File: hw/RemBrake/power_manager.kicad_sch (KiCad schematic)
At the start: 22 parts, among them IC1 LTC2943IDD#TRPBF, Q10 BC337, Q11 BC847, U7 MAX40200AUK, U8 MAX40200AUK

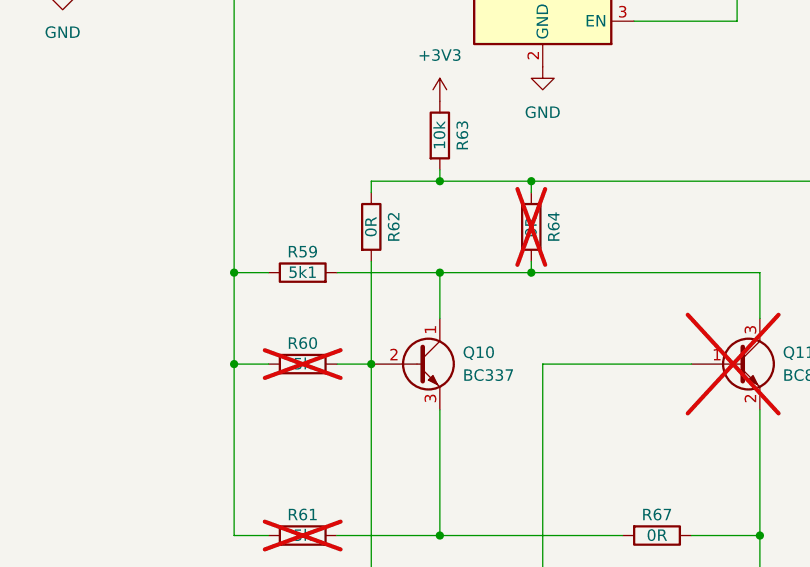
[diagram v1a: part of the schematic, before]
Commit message: adjusted connections to be able to use bc337
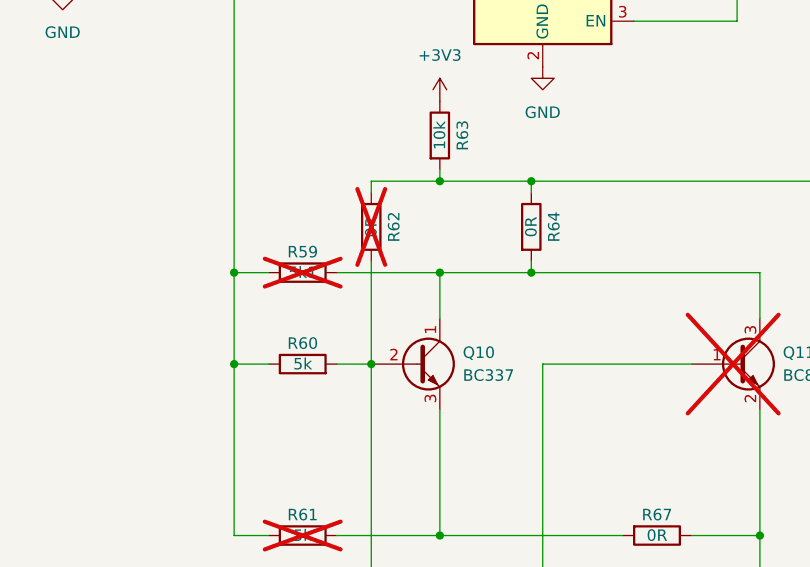
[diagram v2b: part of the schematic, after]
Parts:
- R59, R62: now not fitted; now left out of the parts list
- R60, R64: now fitted; now in the parts list
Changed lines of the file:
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@@
 (kicad_sch
-	(version 20250318)
+	(version 20250513)
 	(generator "eeschema")
 	(generator_version "9.99")
@@
 		(unit 1)
 		(exclude_from_sim no)
-		(in_bom yes)
+		(in_bom no)
 		(on_board yes)
-		(dnp no)
+		(dnp yes)
 		(property "Reference" "R62"
 			(at 195.58 97.79 90)
@@
 		(unit 1)
 		(exclude_from_sim no)
-		(in_bom yes)
+		(in_bom no)
 		(on_board yes)
-		(dnp no)
+		(dnp yes)
 		(property "Reference" "R59"
 			(at 185.42 100.584 90)
@@
 		(unit 1)
 		(exclude_from_sim no)
-		(in_bom no)
+		(in_bom yes)
 		(on_board yes)
-		(dnp yes)
+		(dnp no)
 		(property "Reference" "R60"
 			(at 185.42 110.744 90)
@@
 		(dnp no)
 		(fields_autoplaced yes)
-		(property "Height" "0.8"
-			(at 52.07 -337.77 0)
-			(hide yes)
+		(property "Reference" "IC1"
+			(at 83.82 68.58 0)
 			(effects
 				(font
 					(size 1.27 1.27)
 				)
-				(justify left top)
 			)
 		)
-		(property "Mouser Part Number" "584-LTC2943IDD#TRPBF"
-			(at 52.07 -437.77 0)
-			(hide yes)
+		(property "Value" "LTC2943IDD#TRPBF"
+			(at 83.82 71.12 0)
 			(effects
 				(font
 					(size 1.27 1.27)
 				)
-				(justify left top)
 			)
 		)
-		(property "Mouser Price/Stock" "https://www.mouser.co.uk/ProductDetail/Analog-Devices/LTC2943IDDTRPBF?qs=hVkxg5c3xu8j%252BJ6DK3jV8w%3D%3D"
-			(at 52.07 -537.77 0)
+		(property "Footprint" "Package_DFN_QFN:DFN-8-1EP_3x3mm_P0.5mm_EP1.66x2.38mm"
+			(at 52.07 -37.77 0)
 			(hide yes)
 			(effects
@@
 			)
 		)
-		(property "Manufacturer_Name" "Analog Devices"
-			(at 52.07 -637.77 0)
+		(property "Datasheet" "https://www.mouser.in/datasheet/2/609/2943fa-1271567.pdf"
+			(at 52.07 -137.77 0)
 			(hide yes)
 			(effects
@@
 			)
 		)
-		(property "Manufacturer_Part_Number" "LTC2943IDD#TRPBF"
-			(at 52.07 -737.77 0)
+		(property "Description" "Battery Management 20V Battery Gas Gauge with Voltage, Current & Temperature Measurement"
+			(at 83.82 57.15 0)
 			(hide yes)
 			(effects
@@
 					(size 1.27 1.27)
 				)
-				(justify left top)
 			)
 		)
-		(property "Reference" "IC1"
-			(at 83.82 68.58 0)
+		(property "Height" "0.8"
+			(at 52.07 -337.77 0)
+			(hide yes)
 			(effects
 				(font
 					(size 1.27 1.27)
 				)
+				(justify left top)
 			)
 		)
-		(property "Value" "LTC2943IDD#TRPBF"
-			(at 83.82 71.12 0)
+		(property "Mouser Part Number" "584-LTC2943IDD#TRPBF"
+			(at 52.07 -437.77 0)
+			(hide yes)
 			(effects
 				(font
 					(size 1.27 1.27)
 				)
+				(justify left top)
 			)
 		)
-		(property "Footprint" "Package_DFN_QFN:DFN-8-1EP_3x3mm_P0.5mm_EP1.66x2.38mm"
-			(at 52.07 -37.77 0)
+		(property "Mouser Price/Stock" "https://www.mouser.co.uk/ProductDetail/Analog-Devices/LTC2943IDDTRPBF?qs=hVkxg5c3xu8j%252BJ6DK3jV8w%3D%3D"
+			(at 52.07 -537.77 0)
 			(hide yes)
 			(effects
@@
 			)
 		)
-		(property "Datasheet" "https://www.mouser.in/datasheet/2/609/2943fa-1271567.pdf"
-			(at 52.07 -137.77 0)
+		(property "Manufacturer_Name" "Analog Devices"
+			(at 52.07 -637.77 0)
 			(hide yes)
 			(effects
@@
 			)
 		)
-		(property "Description" "Battery Management 20V Battery Gas Gauge with Voltage, Current & Temperature Measurement"
-			(at 83.82 57.15 0)
+		(property "Manufacturer_Part_Number" "LTC2943IDD#TRPBF"
+			(at 52.07 -737.77 0)
 			(hide yes)
 			(effects
@@
 					(size 1.27 1.27)
 				)
+				(justify left top)
 			)
 		)
@@
 		(unit 1)
 		(exclude_from_sim no)
-		(in_bom no)
+		(in_bom yes)
 		(on_board yes)
-		(dnp yes)
+		(dnp no)
 		(property "Reference" "R64"
 			(at 213.36 97.79 90)

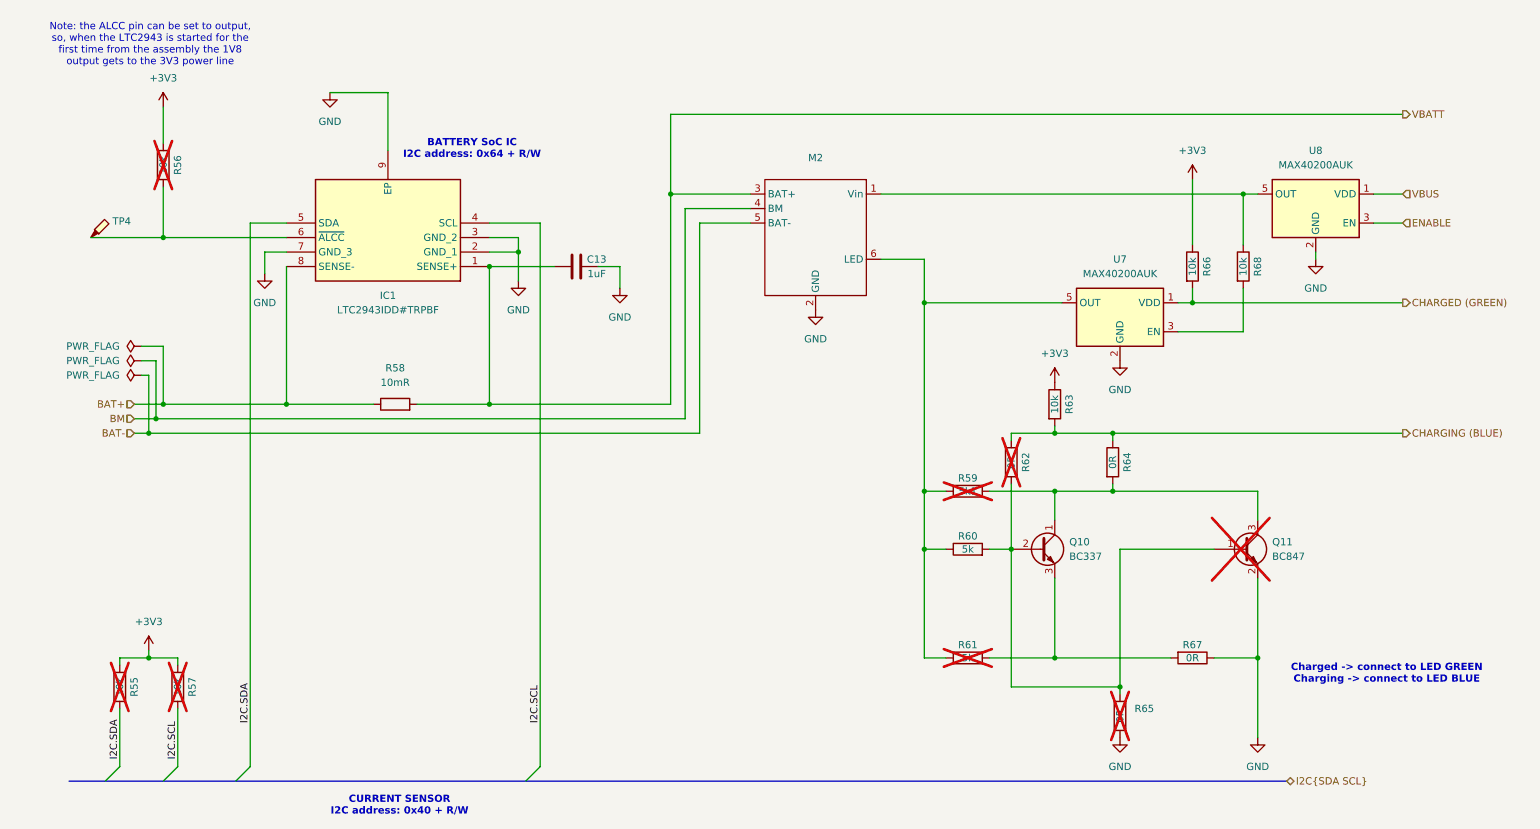
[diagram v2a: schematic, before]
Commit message: finished todos - prepared for routing
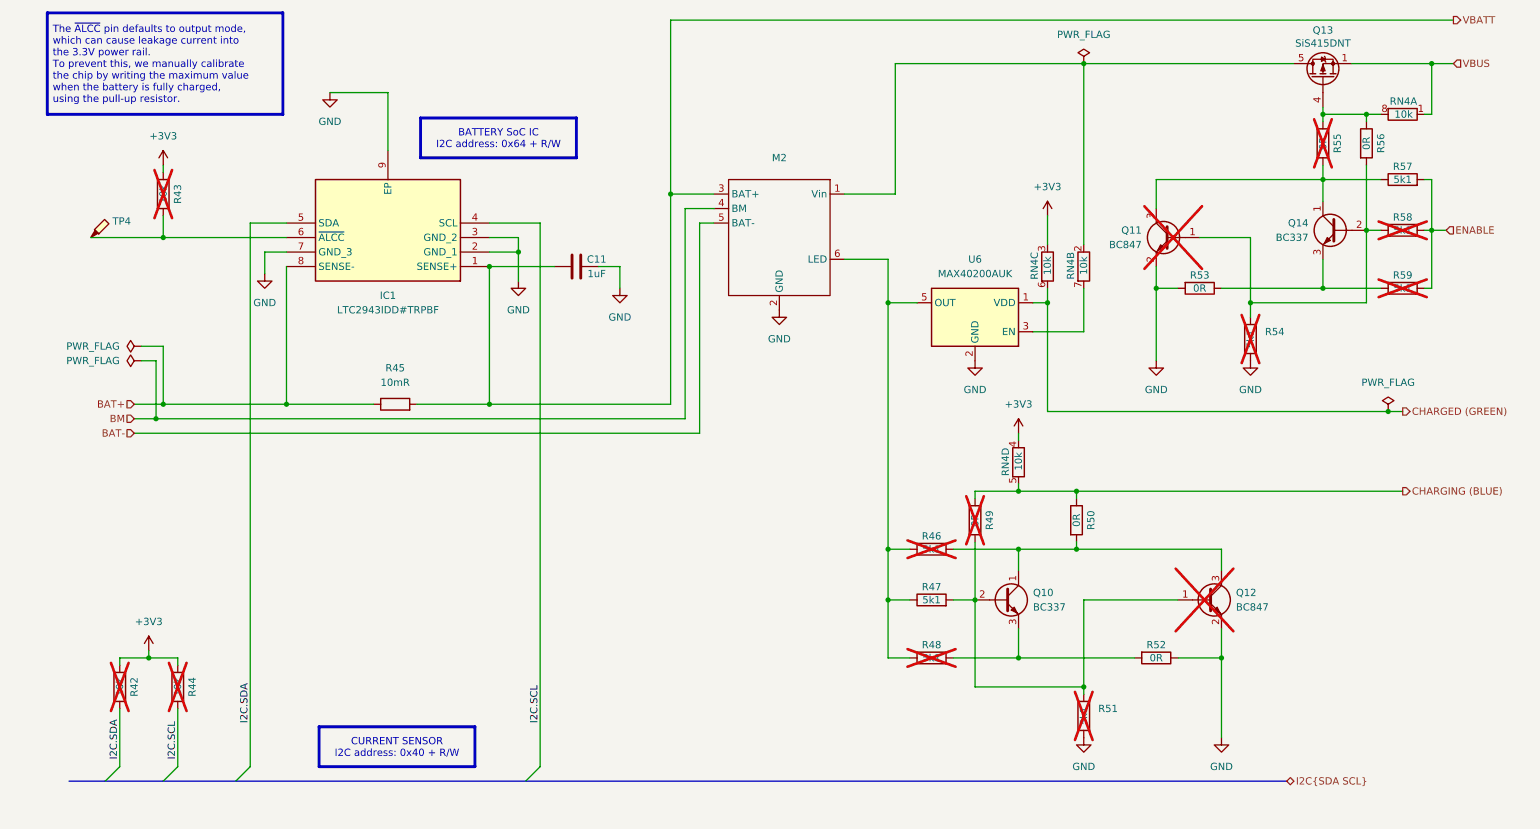
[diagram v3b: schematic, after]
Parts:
- removed R63, R66, R68: 10k, Resistor_SMD:R_0805_2012Metric_Pad1.20x1.40mm_HandSolder, symbol Device:R
- removed U8: MAX40200AUK, Package_TO_SOT_SMD:SOT-23-5, symbol Analog_Switch:MAX40200AUK
- added Q11: BC847, Package_TO_SOT_SMD:SOT-23, symbol Transistor_BJT:BC847
- added Q13: SiS415DNT, Package_SO:Vishay_PowerPAK_1212-8_Single, symbol Transistor_FET:SiS415DNT
- added Q14: BC337, Package_TO_SOT_THT:TO-92_Inline, symbol Transistor_BJT:BC337
- added R53, R55, R56: 0R, Resistor_SMD:R_0805_2012Metric_Pad1.20x1.40mm_HandSolder, symbol Device:R
- added R54, R57, R58, R59: 5k1, Resistor_SMD:R_0805_2012Metric_Pad1.20x1.40mm_HandSolder, symbol Device:R
- added RN4: 10k, Resistor_SMD:R_Array_Convex_4x0603, symbol Device:R_Pack04_Split
- R47: renamed from R60; value 5k -> 5k1
- R48: renamed from R61; value 5k -> 5k1
- R51: renamed from R65; value 0R -> 5k1
- renumbered C13 to C11, Q11 to Q12, R55 to R42, R56 to R43, R57 to R44, R58 to R45, R59 to R46, R62 to R49, R64 to R50, R67 to R52, U7 to U6
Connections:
- net +3V3: now also RN4.3 (R3.1), RN4.4 (R4.1)
- net CHARGED (GREEN): now also RN4.6 (R3.2)
- net CHARGING (BLUE): now also RN4.5 (R4.2)
- net ENABLE: now also R57.2, R58.2, R59.2
- net GND: now also Q11.2 (E), R53.2, R54.1
- net VBUS: now also Q13.1 (S), Q13.2 (S), Q13.3 (S), RN4.1 (R1.1)
- net at M2.1 (Vin): now also Q13.5 (D), RN4.2 (R2.1)
- net at U6.3 (EN): now also RN4.7 (R2.2)
- new net: Q13.4 (G), R55.1, R56.1, RN4.8 (R1.2)
- new net: Q11.3 (C), Q14.1 (C), R55.2, R57.1
- new net: Q14.3 (E), R53.1, R59.1
- new net: Q11.1 (B), Q14.2 (B), R54.2, R56.2, R58.1
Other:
- note removed: "BATTERY SoC IC I2C address: 0x64 + R/W"
- note removed: "CURRENT SENSOR I2C address: 0x40 + R/W"
- note removed: "Charged -> connect to LED GREEN Charging -> connect to LED BLUE"
- note removed: "Note: the ALCC pin can be set to output, so, when the LTC2943 is started for the first time from the assembly the 1V8 output gets to the 3V3 power line"
- moved on the sheet: M2, Q10, R43, R46, R47, R48, R49, R50, R51, R52, U6

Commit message: new routing version 3.0 with power mosfet swich for the charger and fixed problems with LED and buzzer reset delayed circuit
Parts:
- renumbered C11 to C13, R42 to R48, R43 to R49, R44 to R50, R45 to R51, R46 to R52, R47 to R53, R48 to R54, R49 to R55, R50 to R56, R51 to R57, R52 to R58, R53 to R59, R54 to R60, R55 to R61, R56 to R62, R57 to R63, R58 to R64, R59 to R65, U6 to U7
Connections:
- net +3V3: now also RN4.5 (R4.2), RN4.6 (R3.2); no longer RN4.3 (R3.1), RN4.4 (R4.1)
- net CHARGED (GREEN): now also RN4.4 (R4.1); no longer RN4.6 (R3.2)
- net CHARGING (BLUE): now also RN4.3 (R3.1); no longer RN4.5 (R4.2)
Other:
- moved on the sheet: RN4C, RN4D

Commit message: added resistor for the ideal diode enable and new annotation
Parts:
- renumbered R48 to R49, R49 to R50, R50 to R51, R51 to R52, R52 to R53, R53 to R54, R54 to R55, R55 to R56, R56 to R57, R57 to R58, R58 to R59, R59 to R60, R60 to R61, R61 to R62, R62 to R63, R63 to R64, R64 to R65, R65 to R66

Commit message: bms chip layout and adjacent components adjusted
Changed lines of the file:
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@@
 		(dnp no)
 		(property "Reference" "RN4"
-			(at 201.676 66.04 90)
+			(at 197.358 66.294 90)
 			(effects
 				(font

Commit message: finished new version of pcb with transistors gating vbus and fixed ledbar functionality
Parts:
- renumbered IC1 to U7, U7 to U8
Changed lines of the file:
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@@
 		(dnp no)
 		(fields_autoplaced yes)
-		(property "Reference" "IC1"
+		(property "Reference" "U7"
 			(at 83.82 68.58 0)
 			(effects
@@
 			(project "RemBrake"
 				(path "/e6d4ae5b-c9d7-4cbe-b288-c929fdf55a75/65dd8b54-1c0a-4683-aa46-51c439d49612"
-					(reference "IC1")
+					(reference "U7")
 					(unit 1)
 				)
@@
 		(on_board yes)
 		(dnp no)
-		(property "Reference" "U7"
+		(property "Reference" "U8"
 			(at 186.69 62.23 0)
 			(effects
@@
 			(project "RemBrake"
 				(path "/e6d4ae5b-c9d7-4cbe-b288-c929fdf55a75/65dd8b54-1c0a-4683-aa46-51c439d49612"
-					(reference "U7")
-					(unit 1)
-				)
+					(reference "U8")
+					(unit 1)
+				)

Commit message: updated schematics and pcb - smd transistor was not connected to resistor to limit current through buzzer
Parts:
- Q10, Q14, R59, R60, R63, R64: now not fitted; now left out of the parts list
- Q11, Q12, R65: now fitted; now in the parts list
- R49, R51: now fitted
- R62: value 0R -> 10k; now fitted; now in the parts list
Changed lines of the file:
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@@
 	)
 	(hierarchical_label "CHARGING (BLUE)"
-		(shape output)
+		(shape input)
 		(at 261.62 102.87 0)
 		(effects
@@
 	)
 	(hierarchical_label "CHARGED (GREEN)"
-		(shape output)
+		(shape input)
 		(at 261.62 88.9 0)
 		(effects
@@
 		(in_bom yes)
 		(on_board yes)
-		(dnp yes)
+		(dnp no)
 		(property "Reference" "R51"
 			(at 49.53 137.16 90)
@@
 		(unit 1)
 		(exclude_from_sim no)
-		(in_bom no)
+		(in_bom yes)
 		(on_board yes)
-		(dnp yes)
+		(dnp no)
 		(property "Reference" "R62"
 			(at 250.19 41.91 90)
@@
 			)
 		)
-		(property "Value" "0R"
+		(property "Value" "10k"
 			(at 247.65 41.91 90)
 			(effects
@@
 		(unit 1)
 		(exclude_from_sim no)
-		(in_bom yes)
+		(in_bom no)
 		(on_board yes)
-		(dnp no)
+		(dnp yes)
 		(property "Reference" "R59"
 			(at 218.44 129.794 90)
@@
 		(unit 1)
 		(exclude_from_sim no)
-		(in_bom no)
+		(in_bom yes)
 		(on_board yes)
-		(dnp yes)
+		(dnp no)
 		(fields_autoplaced yes)
 		(property "Reference" "Q12"
@@
 		(unit 1)
 		(exclude_from_sim no)
-		(in_bom yes)
+		(in_bom no)
 		(on_board yes)
-		(dnp no)
+		(dnp yes)
 		(property "Reference" "Q14"
 			(at 245.11 55.8799 0)
@@
 		(unit 1)
 		(exclude_from_sim no)
-		(in_bom yes)
+		(in_bom no)
 		(on_board yes)
-		(dnp no)
+		(dnp yes)
 		(property "Reference" "R60"
 			(at 226.06 65.024 90)
@@
 		(unit 1)
 		(exclude_from_sim no)
-		(in_bom no)
+		(in_bom yes)
 		(on_board yes)
-		(dnp yes)
+		(dnp no)
 		(property "Reference" "R65"
 			(at 261.62 54.864 90)
@@
 		(unit 1)
 		(exclude_from_sim no)
-		(in_bom yes)
+		(in_bom no)
 		(on_board yes)
-		(dnp no)
+		(dnp yes)
 		(fields_autoplaced yes)
 		(property "Reference" "Q10"
@@
 		(unit 1)
 		(exclude_from_sim no)
-		(in_bom yes)
+		(in_bom no)
 		(on_board yes)
-		(dnp no)
+		(dnp yes)
 		(property "Reference" "R64"
 			(at 261.62 45.974 90)
@@
 		(in_bom yes)
 		(on_board yes)
-		(dnp yes)
+		(dnp no)
 		(property "Reference" "R49"
 			(at 39.37 137.16 90)
@@
 		(unit 1)
 		(exclude_from_sim no)
-		(in_bom yes)
+		(in_bom no)
 		(on_board yes)
-		(dnp no)
+		(dnp yes)
 		(property "Reference" "R63"
 			(at 257.81 41.91 90)
@@
 		(unit 1)
 		(exclude_from_sim no)
-		(in_bom no)
+		(in_bom yes)
 		(on_board yes)
-		(dnp yes)
+		(dnp no)
 		(property "Reference" "Q11"
 			(at 215.9 57.1499 0)
